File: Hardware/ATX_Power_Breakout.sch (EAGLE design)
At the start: 13 parts

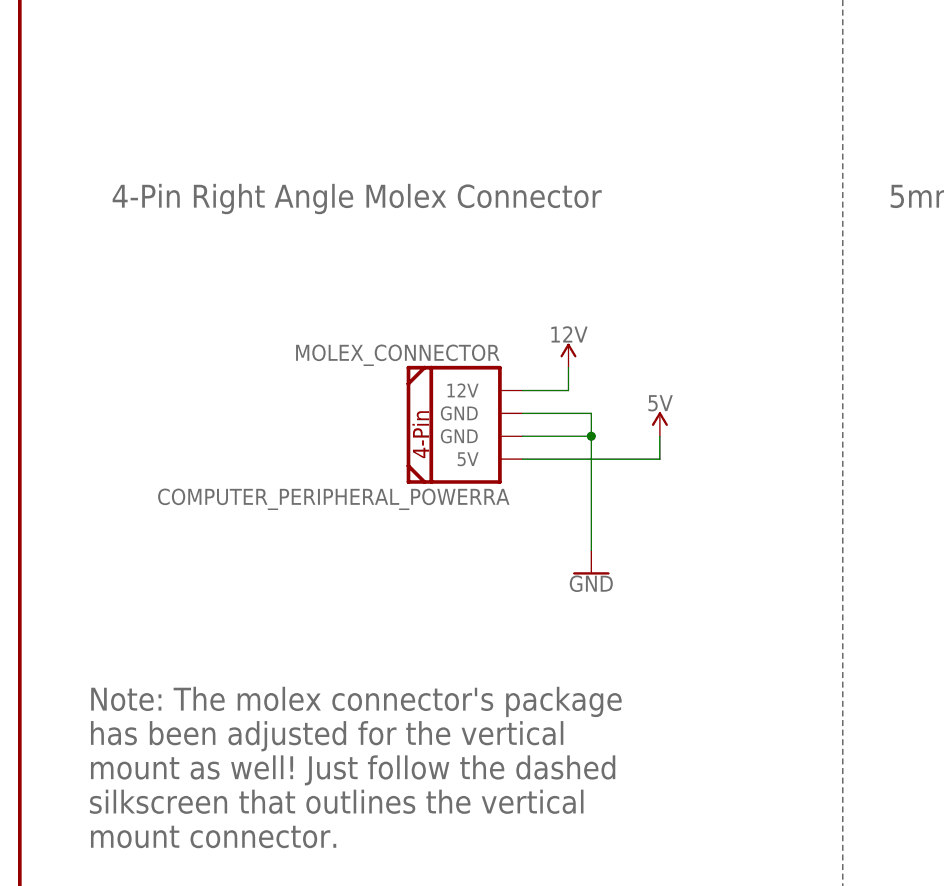
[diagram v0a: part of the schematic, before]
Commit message: Rename Board and Files
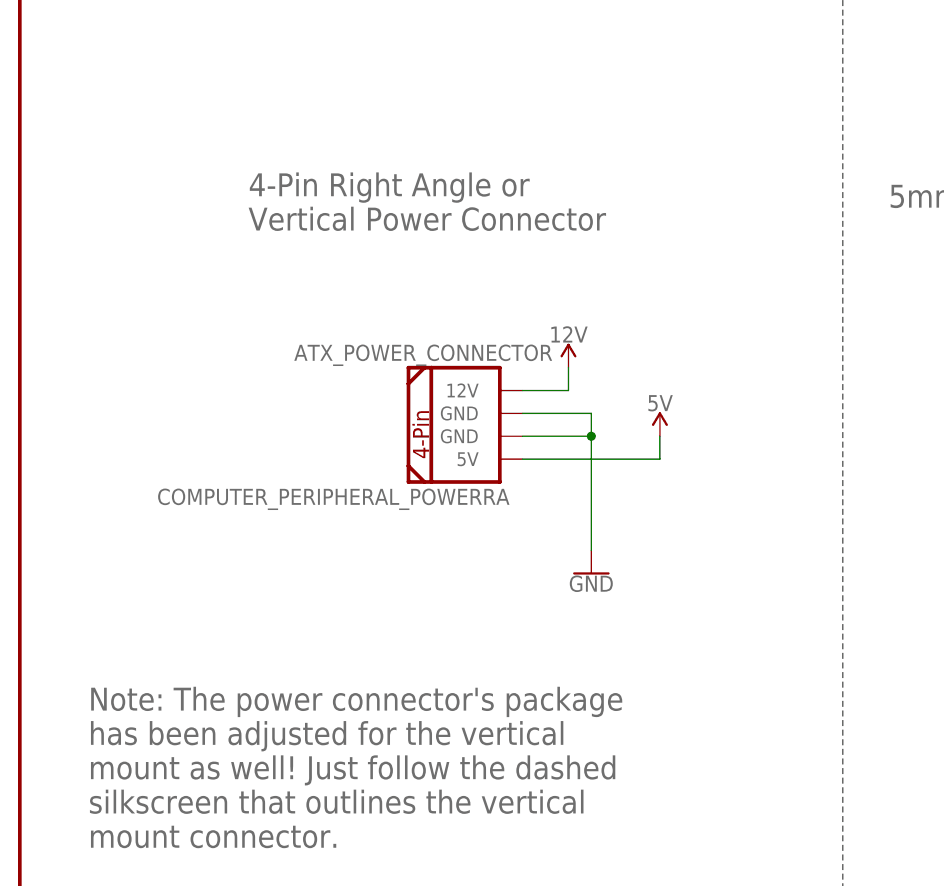
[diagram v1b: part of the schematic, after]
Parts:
- renumbered MOLEX_CONNECTOR to ATX_POWER_CONNECTOR
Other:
- note added: "4-Pin Right Angle or Vertical Power Connector"
- note added: "Note: The power connector's package has been adjusted for the vertical mount as well! Just follow the dashed silkscreen that outlines the vertical mount connector."
- note removed: "4-Pin Right Angle Molex Connector"
- note removed: "Note: The molex connector's package has been adjusted for the vertical mount as well! Just follow the dashed silkscreen that outlines the vertical mount connector."
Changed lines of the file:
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@@
 <parts>
 <part name="FRAME1" library="SparkFun-Aesthetics" deviceset="FRAME-LETTER" device=""/>
-<part name="MOLEX_CONNECTOR" library="SparkFun-Retired" deviceset="COMPUTER_PERIPHERAL_POWER" device="RA"/>
+<part name="ATX_POWER_CONNECTOR" library="SparkFun-Retired" deviceset="COMPUTER_PERIPHERAL_POWER" device="RA"/>
 <part name="LOGO1" library="SparkFun-Aesthetics" deviceset="OSHW-LOGO" device="S"/>
 <part name="LOGO2" library="SparkFun-Aesthetics" deviceset="SFE_LOGO_NAME_FLAME" device=".1_INCH"/>
@@
 <text x="96.52" y="134.62" size="2.54" layer="95" font="vector" ratio="15">5mm Screw Terminals</text>
 <text x="177.8" y="99.06" size="2.54" layer="95" font="vector" ratio="15">0.1" PTH Header Pins</text>
-<text x="10.16" y="134.62" size="2.54" layer="95" font="vector" ratio="15">4-Pin Right Angle Molex Connector</text>
+<text x="25.4" y="132.08" size="2.54" layer="95" font="vector" ratio="15">4-Pin Right Angle or
+Vertical Power Connector</text>
 <wire x1="91.44" y1="185.42" x2="91.44" y2="0" width="0.1524" layer="97" style="shortdash"/>
 <wire x1="147.32" y1="185.42" x2="147.32" y2="116.84" width="0.2032" layer="95" style="shortdash"/>
@@
 <wire x1="147.32" y1="116.84" x2="147.32" y2="35.56" width="0.1524" layer="97" style="shortdash"/>
 <wire x1="147.32" y1="116.84" x2="248.92" y2="116.84" width="0.1524" layer="97" style="shortdash"/>
-<text x="7.62" y="63.5" size="2.54" layer="95" font="vector" ratio="15">Note: The molex connector's package
+<text x="7.62" y="63.5" size="2.54" layer="95" font="vector" ratio="15">Note: The power connector's package
 has been adjusted for the vertical
 mount as well! Just follow the dashed
@@
 <instance part="FRAME1" gate="G$1" x="0" y="0"/>
 <instance part="FRAME1" gate="V" x="147.32" y="0"/>
-<instance part="MOLEX_CONNECTOR" gate="G$1" x="48.26" y="111.76" smashed="yes">
+<instance part="ATX_POWER_CONNECTOR" gate="G$1" x="48.26" y="111.76" smashed="yes">
 <attribute name="VALUE" x="15.24" y="101.6" size="1.778" layer="96" font="vector" ratio="15"/>
 <attribute name="NAME" x="30.48" y="117.602" size="1.778" layer="95" font="vector" ratio="15"/>
@@
 <net name="12V" class="0">
 <segment>
-<pinref part="MOLEX_CONNECTOR" gate="G$1" pin="12V"/>
+<pinref part="ATX_POWER_CONNECTOR" gate="G$1" pin="12V"/>
 <wire x1="55.88" y1="114.3" x2="60.96" y2="114.3" width="0.1524" layer="91"/>
 <wire x1="60.96" y1="114.3" x2="60.96" y2="116.84" width="0.1524" layer="91"/>
@@
 <net name="GND" class="0">
 <segment>
-<pinref part="MOLEX_CONNECTOR" gate="G$1" pin="GND@2"/>
+<pinref part="ATX_POWER_CONNECTOR" gate="G$1" pin="GND@2"/>
 <wire x1="55.88" y1="109.22" x2="63.5" y2="109.22" width="0.1524" layer="91"/>
 <wire x1="63.5" y1="109.22" x2="63.5" y2="96.52" width="0.1524" layer="91"/>
 <pinref part="GND1" gate="1" pin="GND"/>
-<pinref part="MOLEX_CONNECTOR" gate="G$1" pin="GND@1"/>
+<pinref part="ATX_POWER_CONNECTOR" gate="G$1" pin="GND@1"/>
 <wire x1="63.5" y1="111.76" x2="55.88" y2="111.76" width="0.1524" layer="91"/>
 <wire x1="63.5" y1="111.76" x2="63.5" y2="109.22" width="0.1524" layer="91"/>
@@
 <net name="5V" class="0">
 <segment>
-<pinref part="MOLEX_CONNECTOR" gate="G$1" pin="5V"/>
+<pinref part="ATX_POWER_CONNECTOR" gate="G$1" pin="5V"/>
 <wire x1="55.88" y1="106.68" x2="71.12" y2="106.68" width="0.1524" layer="91"/>
 <pinref part="SUPPLY2" gate="G$1" pin="5V"/>
